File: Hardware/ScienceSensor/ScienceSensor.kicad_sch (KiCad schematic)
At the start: 16 parts

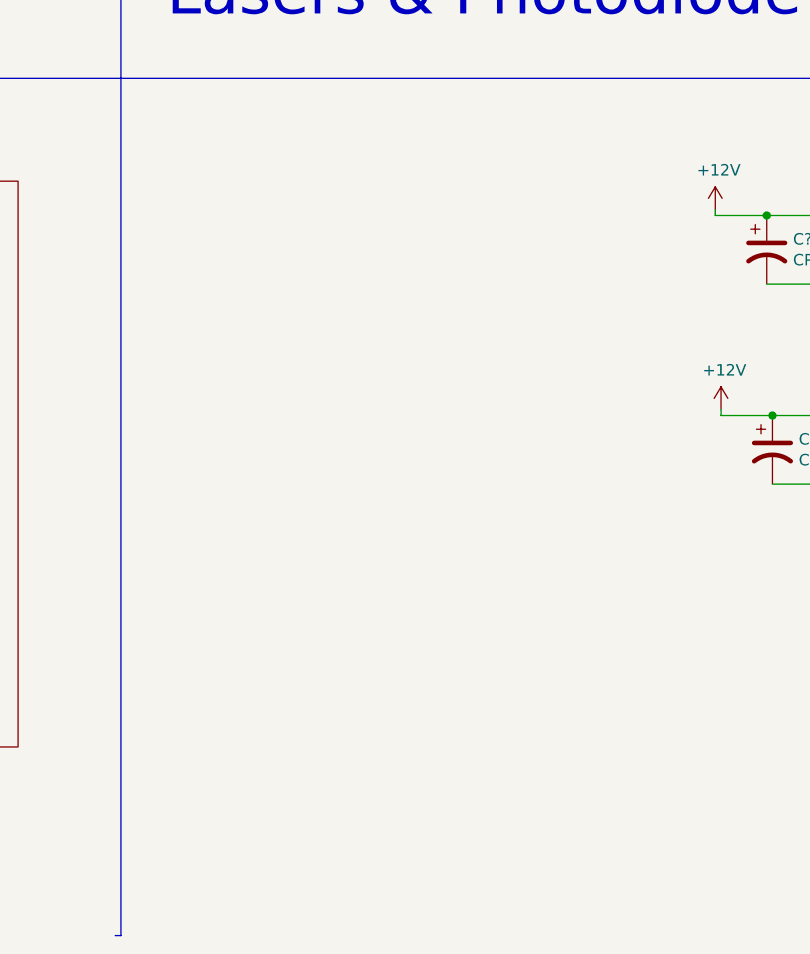
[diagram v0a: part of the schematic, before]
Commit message: Finished limit switch and 12V motor controller with encoder.
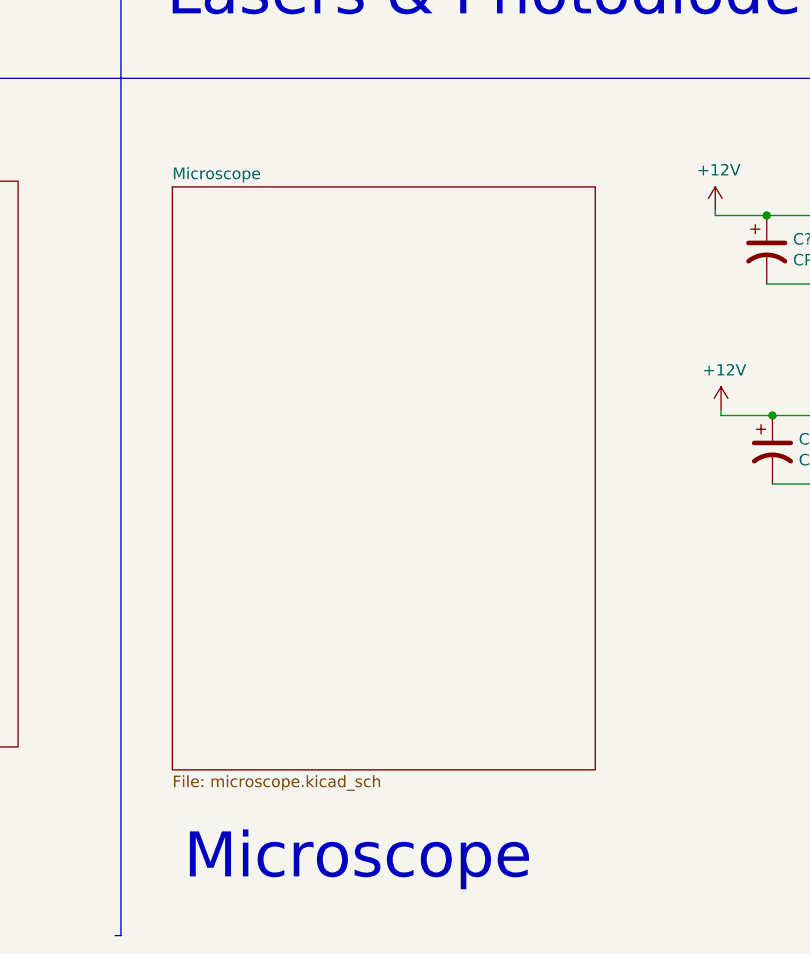
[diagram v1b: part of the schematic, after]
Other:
- added sheet Microscope (microscope.kicad_sch)
- note added: "Microscope"
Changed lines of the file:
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@@
     (effects (font (size 5.0038 5.0038)) (justify left bottom))
+  )
+  (text "Microscope" (at 127 191.77 0)
+    (effects (font (size 5 5)) (justify left bottom))
   )
   (symbol (lib_id "MRDT_Connectors:AndersonPP") (at 217.805 38.735 0) (unit 1)
@@
     )
   )
+  (sheet (at 125.73 114.3) (size 46.99 64.77) (fields_autoplaced)
+    (stroke (width 0.1524) (type solid) (color 0 0 0 0))
+    (fill (color 0 0 0 0.0000))
+    (property "Sheet name" "Microscope" (id 0) (at 125.73 113.5884 0)
+      (effects (font (size 1.27 1.27)) (justify left bottom))
+    )
+    (property "Sheet file" "microscope.kicad_sch" (id 1) (at 125.73 179.6546 0)
+      (effects (font (size 1.27 1.27)) (justify left top))
+    )
+  )
   (sheet_instances
     (path "/" (page "1"))
@@
     (path "/00000000-0000-0000-0000-00006320ec71" (page "3"))
     (path "/00000000-0000-0000-0000-000063213561" (page "4"))
+    (path "/65564703-75e1-467a-8fc4-64921d9171f3" (page "5"))
   )
   (symbol_instances
@@
       (reference "#PWR?") (unit 1) (value "+5V") (footprint "")
     )
+    (path "/65564703-75e1-467a-8fc4-64921d9171f3/2c2b603e-171c-4fea-bb35-1733d6da4820"
+      (reference "#PWR?") (unit 1) (value "+12V") (footprint "")
+    )
     (path "/00000000-0000-0000-0000-00006320eb63/2c753200-a209-4b6d-aa8f-a613a5b3decd"
       (reference "#PWR?") (unit 1) (value "GND") (footprint "")
@@
     )
     (path "/00000000-0000-0000-0000-00006320eb63/5025beac-e26e-4abf-b832-d96750dfc034"
+      (reference "#PWR?") (unit 1) (value "GND") (footprint "")
+    )
+    (path "/65564703-75e1-467a-8fc4-64921d9171f3/541bc36c-7cb7-4c0e-b640-8dc501a76b20"
+      (reference "#PWR?") (unit 1) (value "GND") (footprint "")
+    )
+    (path "/65564703-75e1-467a-8fc4-64921d9171f3/55db6873-102e-4cc6-ab96-a1532f617724"
       (reference "#PWR?") (unit 1) (value "GND") (footprint "")
     )
@@
       (reference "#PWR?") (unit 1) (value "+3V3") (footprint "")
     )
+    (path "/65564703-75e1-467a-8fc4-64921d9171f3/7ebad923-b561-4c92-93a2-500d889de82d"
+      (reference "#PWR?") (unit 1) (value "GND") (footprint "")
+    )
     (path "/00000000-0000-0000-0000-00006320eb63/7f5acf0f-93d4-42f4-8a63-03ada1631a63"
       (reference "#PWR?") (unit 1) (value "+3V3") (footprint "")
@@
       (reference "#PWR?") (unit 1) (value "GND") (footprint "")
     )
+    (path "/65564703-75e1-467a-8fc4-64921d9171f3/85c1f72c-1f96-42e4-b159-69381a088266"
+      (reference "#PWR?") (unit 1) (value "+3.3V") (footprint "")
+    )
     (path "/00000000-0000-0000-0000-00006320eb63/a103f583-b944-4021-ad5f-ca2f4caf3b45"
       (reference "#PWR?") (unit 1) (value "+5V") (footprint "")
@@
       (reference "#PWR?") (unit 1) (value "+3V3") (footprint "")
     )
+    (path "/65564703-75e1-467a-8fc4-64921d9171f3/e8263411-d421-4416-8832-bb38ba8ecc00"
+      (reference "#PWR?") (unit 1) (value "+5VA") (footprint "")
+    )
     (path "/00000000-0000-0000-0000-00006320eb63/e85e67dc-c502-481b-a013-cc5b91602a31"
       (reference "#PWR?") (unit 1) (value "+5V") (footprint "")
@@
       (reference "Conn?") (unit 1) (value "Molex_SL_02") (footprint "")
     )
+    (path "/65564703-75e1-467a-8fc4-64921d9171f3/4b265f75-2d55-405f-a369-a6d67fb4e690"
+      (reference "Conn?") (unit 1) (value "Molex_SL_03") (footprint "MRDT_Connectors:MOLEX_SL_03_Vertical")
+    )
+    (path "/65564703-75e1-467a-8fc4-64921d9171f3/ed4807e9-fafd-4a13-92ec-380bd7dde199"
+      (reference "Conn?") (unit 1) (value "Molex_SL_02") (footprint "MRDT_Connectors:MOLEX_SL_02_Vertical")
+    )
     (path "/00000000-0000-0000-0000-000063214fb6"
       (reference "Conn?") (unit 2) (value "AndersonPP") (footprint "")
@@
       (reference "D?") (unit 1) (value "LED") (footprint "")
     )
+    (path "/65564703-75e1-467a-8fc4-64921d9171f3/58e3cb07-8b72-4217-afa9-459762c3c39a"
+      (reference "D?") (unit 1) (value "Yellow") (footprint "LED_SMD:LED_0603_1608Metric_Pad1.05x0.95mm_HandSolder")
+    )
     (path "/00000000-0000-0000-0000-00006320eb63/4019743e-abfb-4451-82ef-f7a09e940ac4"
       (reference "FB1") (unit 1) (value "Ferrite_Bead") (footprint "")
@@
       (reference "R?") (unit 1) (value "R") (footprint "")
     )
+    (path "/65564703-75e1-467a-8fc4-64921d9171f3/fdd9348a-0cd5-45bb-9500-cf431cc230e6"
+      (reference "R?") (unit 1) (value "120") (footprint "Resistor_SMD:R_0603_1608Metric_Pad0.98x0.95mm_HandSolder")
+    )
+    (path "/65564703-75e1-467a-8fc4-64921d9171f3/70b1c626-0964-4d66-9dc7-1d83712554df"
+      (reference "Servo?") (unit 1) (value "Molex_SL_03") (footprint "")
+    )
     (path "/00000000-0000-0000-0000-00006320eb63/4361c90c-dd26-46c6-b314-bdbe49286a65"
